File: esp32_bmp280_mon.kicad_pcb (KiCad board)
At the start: 2 copper layers, 39.1 x 49.5 mm, 25 parts, among them IC1 TP4056, J1 BMP280, J2 UART, J3 BAT, J4 USB_B_Micro, Q1 MMDT3904, U1 ESP32-WROOM-32, U2 HT78xx

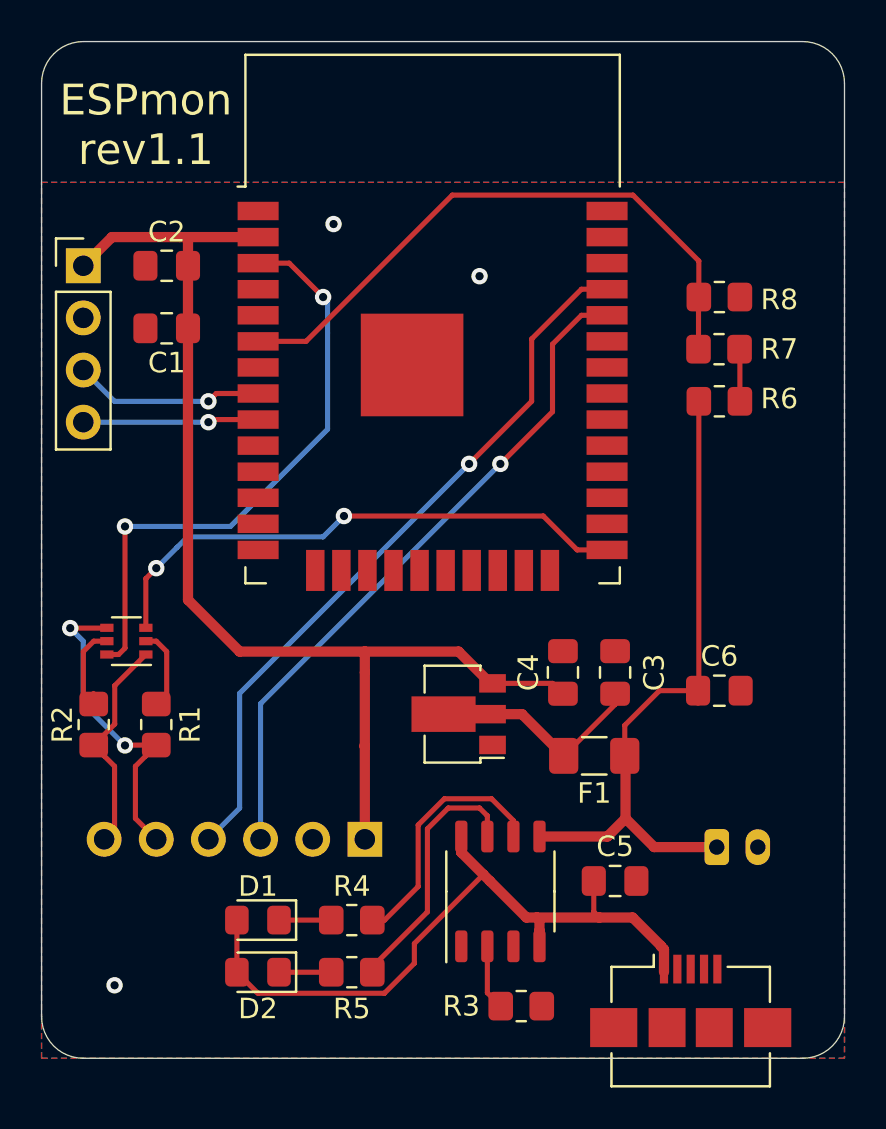
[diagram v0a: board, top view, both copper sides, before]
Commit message: port to SHT40 sensor on board and different LDO and charger
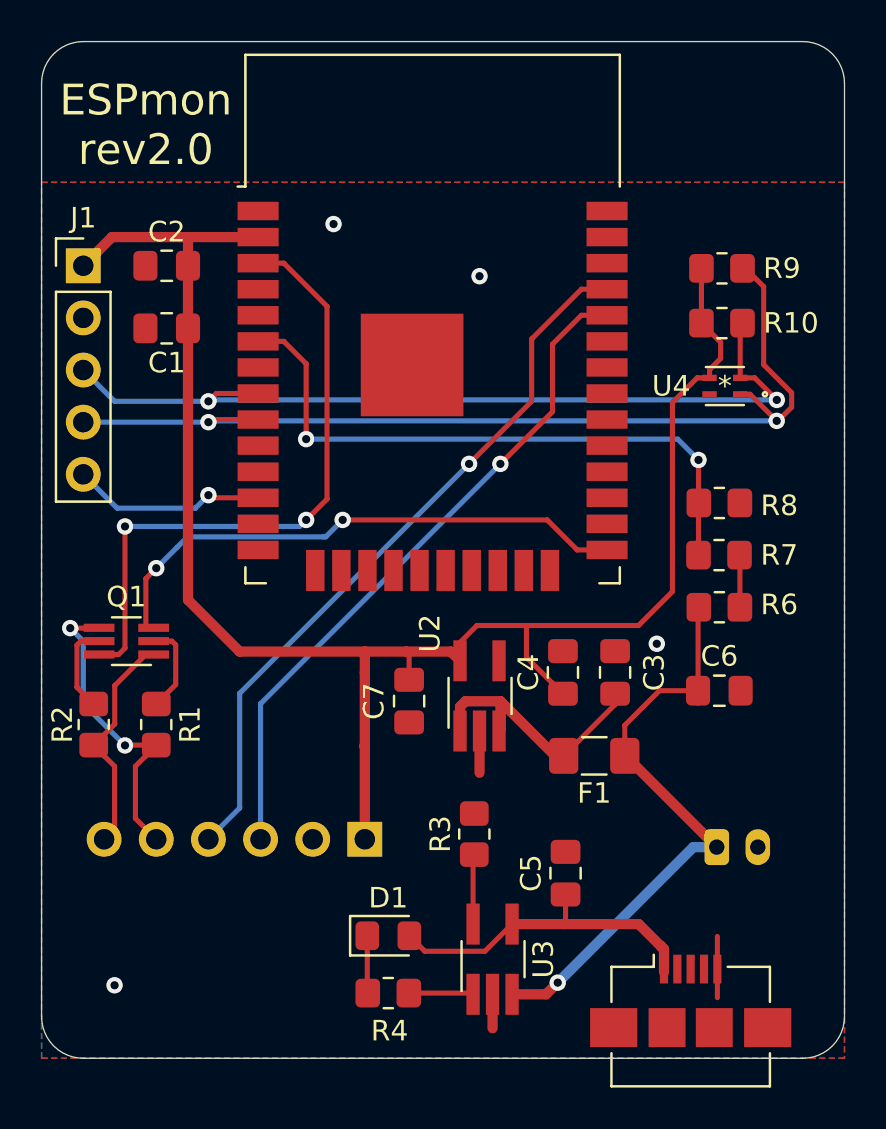
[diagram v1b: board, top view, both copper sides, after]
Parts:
- removed D2: red, Diode_SMD:D_0805_2012Metric_Pad1.15x1.40mm_HandSolder
- removed IC1: TP4056, Package_SO:SSOP-8_3.9x5.05mm_P1.27mm
- removed R5: 1k, Resistor_SMD:R_0805_2012Metric_Pad1.20x1.40mm_HandSolder
- added C7: 100n, Capacitor_SMD:C_0805_2012Metric_Pad1.18x1.45mm_HandSolder, F.Cu at (167.8, 76.6)
- added R10: 10k, Resistor_SMD:R_0805_2012Metric_Pad1.20x1.40mm_HandSolder, F.Cu at (183.0, 58.2)
- added R9: 10k, Resistor_SMD:R_0805_2012Metric_Pad1.20x1.40mm_HandSolder, F.Cu at (183.0, 55.5)
- added U3: STC4054GR, Package_TO_SOT_SMD:TSOT-23-5_HandSoldering, F.Cu at (171.8, 89.2)
- added U4: SHT40-AD1B-R2, SHT40:SHT40-AD1B-R2, F.Cu at (183.1, 61.2)
- C5, C6: value 10nF -> 1uF
- D1: value green -> red
- J1: value BMP280 -> I2C; footprint Connector_PinHeader_2.54mm:PinHeader_1x04_P2.54mm_Vertical -> Connector_PinHeader_2.54mm:PinHeader_1x05_P2.54mm_Vertical
- Q1: footprint Package_TO_SOT_SMD:SOT-363_SC-70-6 -> Package_TO_SOT_SMD:SOT-363_SC-70-6_Handsoldering
- R6, R7: value 2m2 -> 2m
- R8: value 2m2 -> 1m
- U2: value HT78xx -> RT9080-33GJ5; footprint Package_TO_SOT_SMD:SOT-89-3 -> Package_TO_SOT_SMD:TSOT-23-5_HandSoldering
- moved R6 10.0 mm to (182.9, 72.0)
- moved R8 10.0 mm to (182.9, 66.9)
- moved R7 10.0 mm to (182.9, 69.5)
- moved R3 8.69 mm to (170.9, 83.1), turned to 90 degrees
- moved D1 6.40 mm to (166.8, 88.0), turned to 0 degrees
- moved R4 3.98 mm to (166.8, 90.8)
- moved C5 2.44 mm to (175.4, 85.0), turned to 90 degrees
- moved U2 1.35 mm to (171.2, 76.3), turned to 90 degrees
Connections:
- U1 pad 12: Net-(U1-Pad12) -> /IO27
- U2 pad 1: GND -> Net-(C3-Pad1)
- U2 pad 2: Net-(C3-Pad1) -> GND
- U2 pad 3: +3V3 -> Net-(C3-Pad1)
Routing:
- net /IO33: track 8.57 -> 47.4 mm, vias 1 -> 2
- net /IO32: track 9.31 -> 42.0 mm, vias 1 -> 2
- net +3V3: track 56.2 -> 86.4 mm
- net VCC: track 36.6 -> 16.6 mm
- net Net-(IC1-Pad7): track 12.6 -> 0.00 mm
- net /IO27: track 0.00 -> 9.52 mm, vias 0 -> 1
- net Net-(R4-Pad2): track 12.3 -> 3.15 mm
- net GND: track 0.00 -> 6.68 mm, vias 3 -> 4
- net Net-(C3-Pad1): track 8.46 -> 13.3 mm
- net +BATT: track 33.5 -> 30.2 mm, vias 0 -> 1
- net Net-(D2-Pad1): track 2.55 -> 0.00 mm
- net /EN: track 29.2 -> 31.0 mm
- net Net-(Q1-Pad2): track 3.99 -> 4.93 mm
- net /IO34: track 30.1 -> 30.6 mm, vias 0 -> 2
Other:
- board text added: "ESPmon rev2.0"
- board text added: "GPIO 27"
- board text removed: "ESPmon rev1.1"
